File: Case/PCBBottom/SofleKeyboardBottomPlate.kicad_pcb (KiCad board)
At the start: 2 copper layers, 137.2 x 109.2 mm, 9 parts

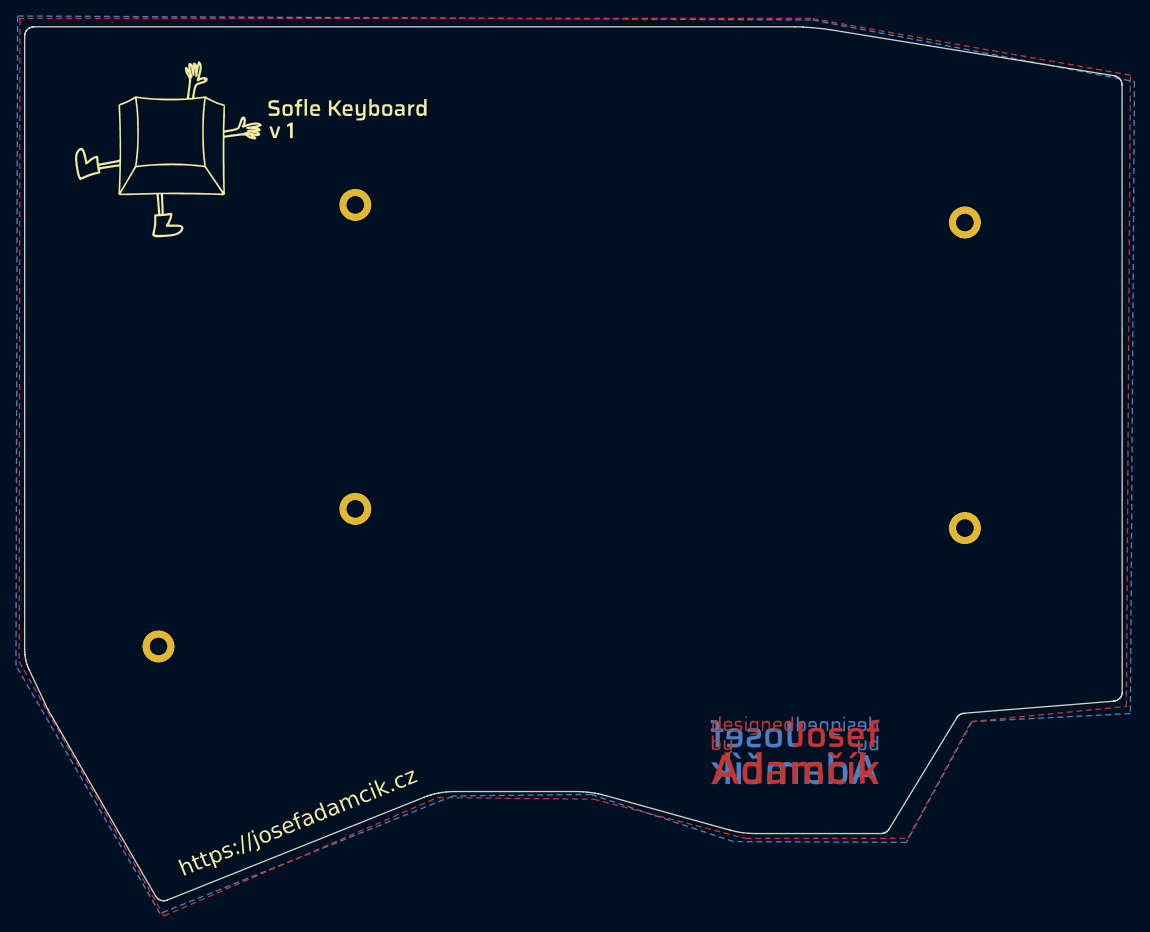
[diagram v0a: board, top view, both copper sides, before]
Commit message: Changed labels on silk screens
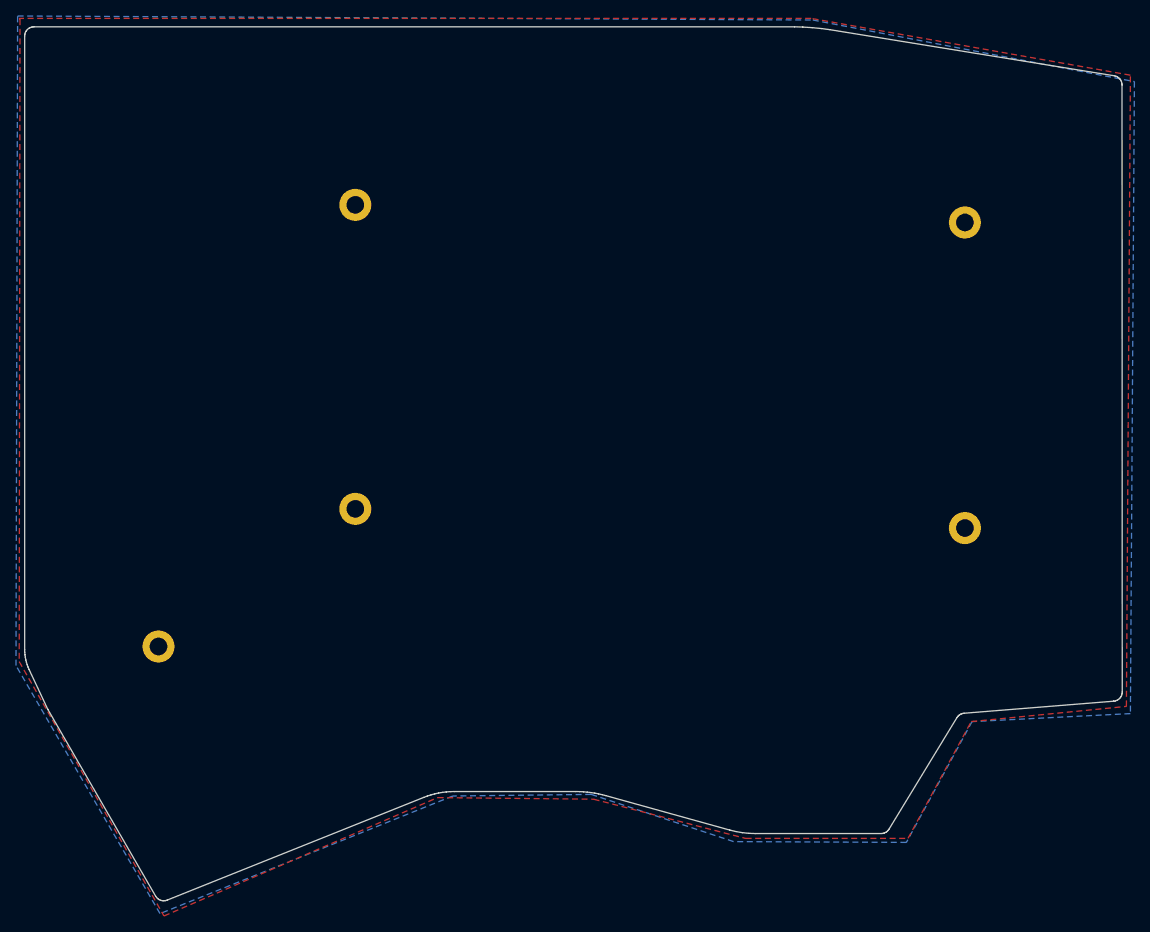
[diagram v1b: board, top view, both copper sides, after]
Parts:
- removed Ref** (x2): Val**, logos:josef_adamcik_20mm_cu_mask
- removed Ref**: Val**, SofleKeyboardBottomPlate:SofleLogo2
- removed Ref**: Val**, SofleKeyboardBottomPlate:SofleLogo1
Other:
- board text removed: "https://josefadamcik.cz"

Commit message: Removed Cu plating on both sides from bottom plate
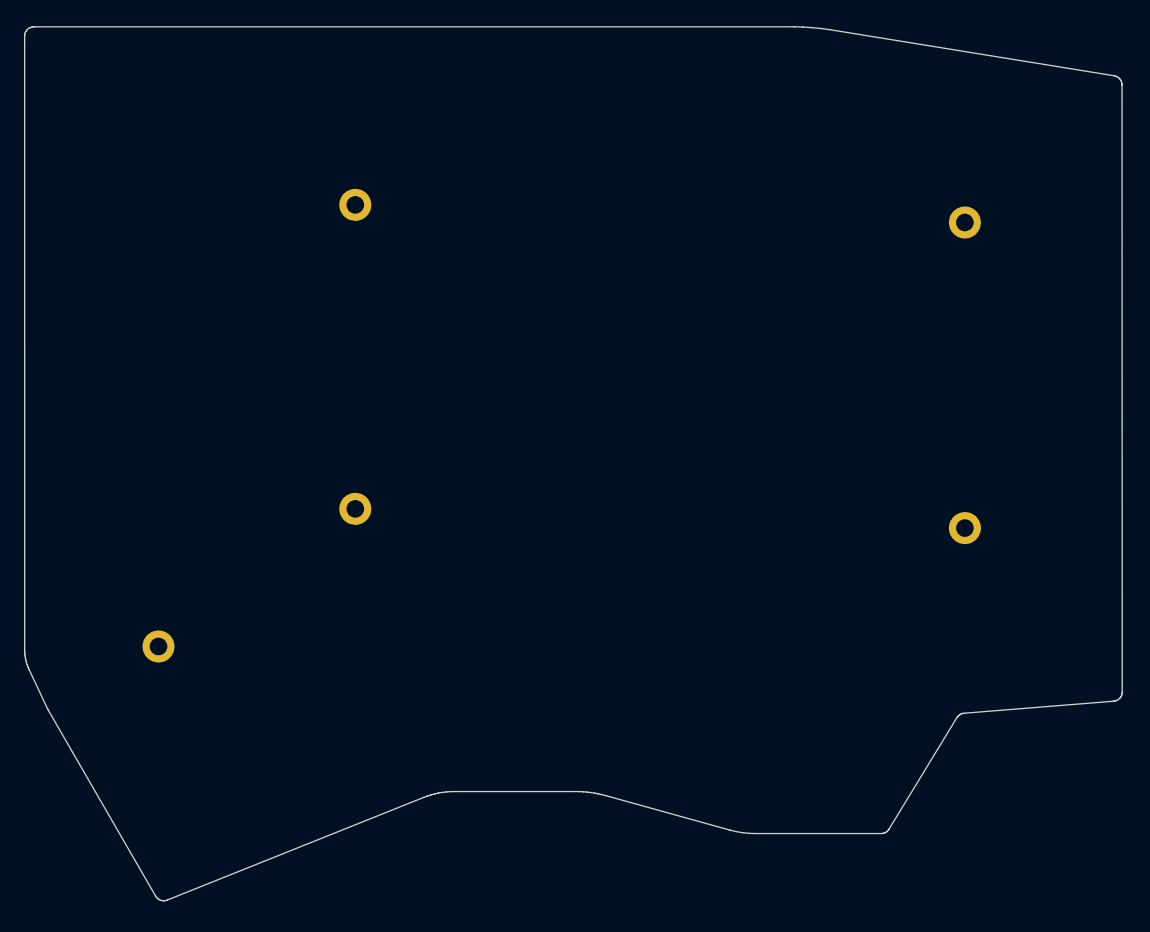
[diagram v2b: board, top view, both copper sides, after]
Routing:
- removed copper zone on B.Cu, net (none)
- removed copper zone on F.Cu, net (none)
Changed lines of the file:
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@@
   (page A4)
   (layers
-    (0 F.Cu signal hide)
-    (31 B.Cu signal)
+    (0 F.Cu signal)
+    (31 B.Cu signal hide)
     (32 B.Adhes user hide)
     (33 F.Adhes user hide)
@@
   (gr_line (start 156.71997 103.850003) (end 156.72 103.850003) (layer Edge.Cuts) (width 0.1))
   (gr_line (start 156.72 103.850003) (end 156.72 103.850003) (layer Edge.Cuts) (width 0.1))
-  (zone (net 0) (net_name "") (layer F.Cu) (hatch edge 0.508)
-    (connect_pads (clearance 0.508))
-    (min_thickness 0.254)
-    (fill yes (arc_segments 32) (thermal_gap 0.508) (thermal_bridge_width 0.508))
-    (polygon
-      (pts
-        (xy 20 18.6) (xy 19.9 98.9) (xy 38 130.7) (xy 72.2 115.9) (xy 91.7 116.1)
-        (xy 110.7 121) (xy 131 121) (xy 138.9 106.4) (xy 158.3 104.5) (xy 158.8 25.6)
-        (xy 118.9 18.5) (xy 19.9 18.5)
-      )
-    )
-  )
-  (zone (net 0) (net_name "") (layer B.Cu) (hatch edge 0.508)
-    (connect_pads (clearance 0.508))
-    (min_thickness 0.254)
-    (fill yes (arc_segments 32) (thermal_gap 0.508) (thermal_bridge_width 0.508))
-    (polygon
-      (pts
-        (xy 19.7 18.2) (xy 119.1 18.7) (xy 159.3 26.4) (xy 158.8 105.4) (xy 139 106.4)
-        (xy 130.8 121.5) (xy 109.2 121.4) (xy 91.4 115.5) (xy 74.1 115.7) (xy 37.5 130.4)
-        (xy 19.5 99.4)
-      )
-    )
-  )
 )
